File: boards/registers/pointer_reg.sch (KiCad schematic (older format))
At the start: 42 parts, among them U10 74ACT161, U11 74ACT244, U12 74ACT244, U13 74ACT161, U14 74ACT161, U15 74ACT244, U16 74ACT244, U9 74ACT161

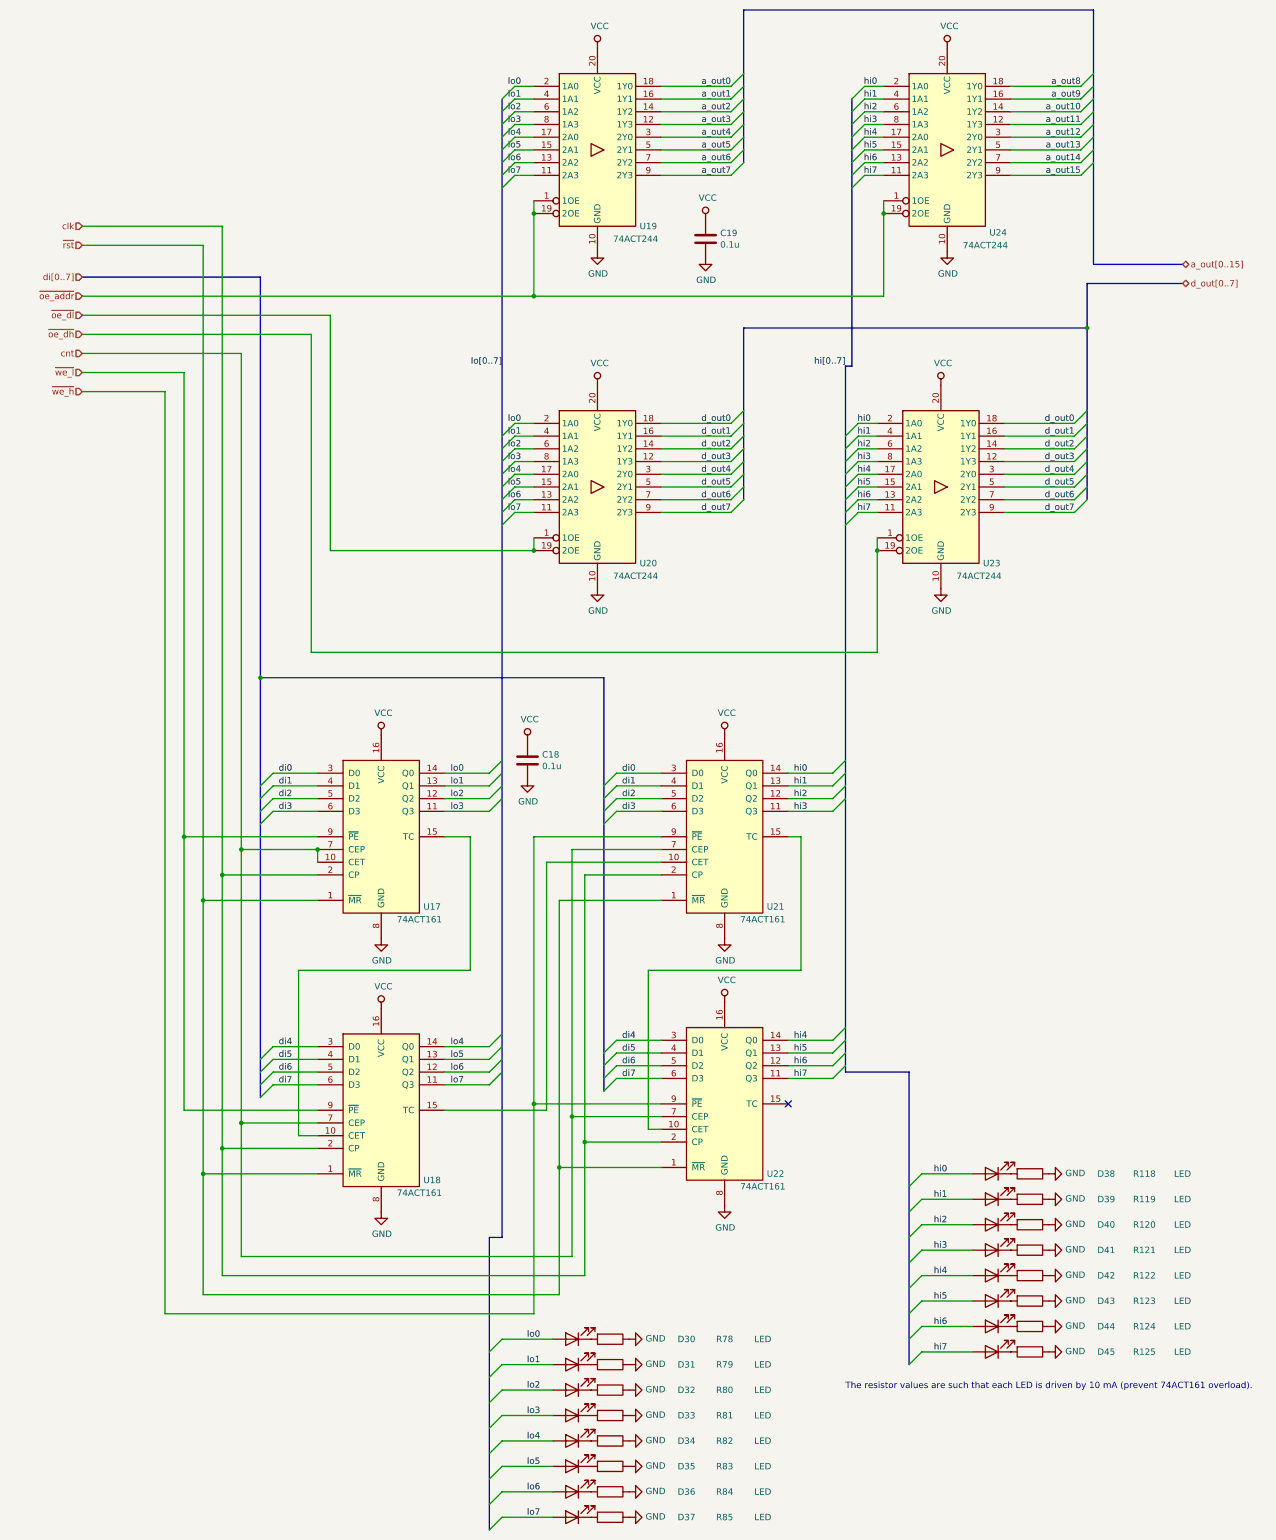
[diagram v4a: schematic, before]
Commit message: Remove RAM and ROM from the registers board, board rework in progress
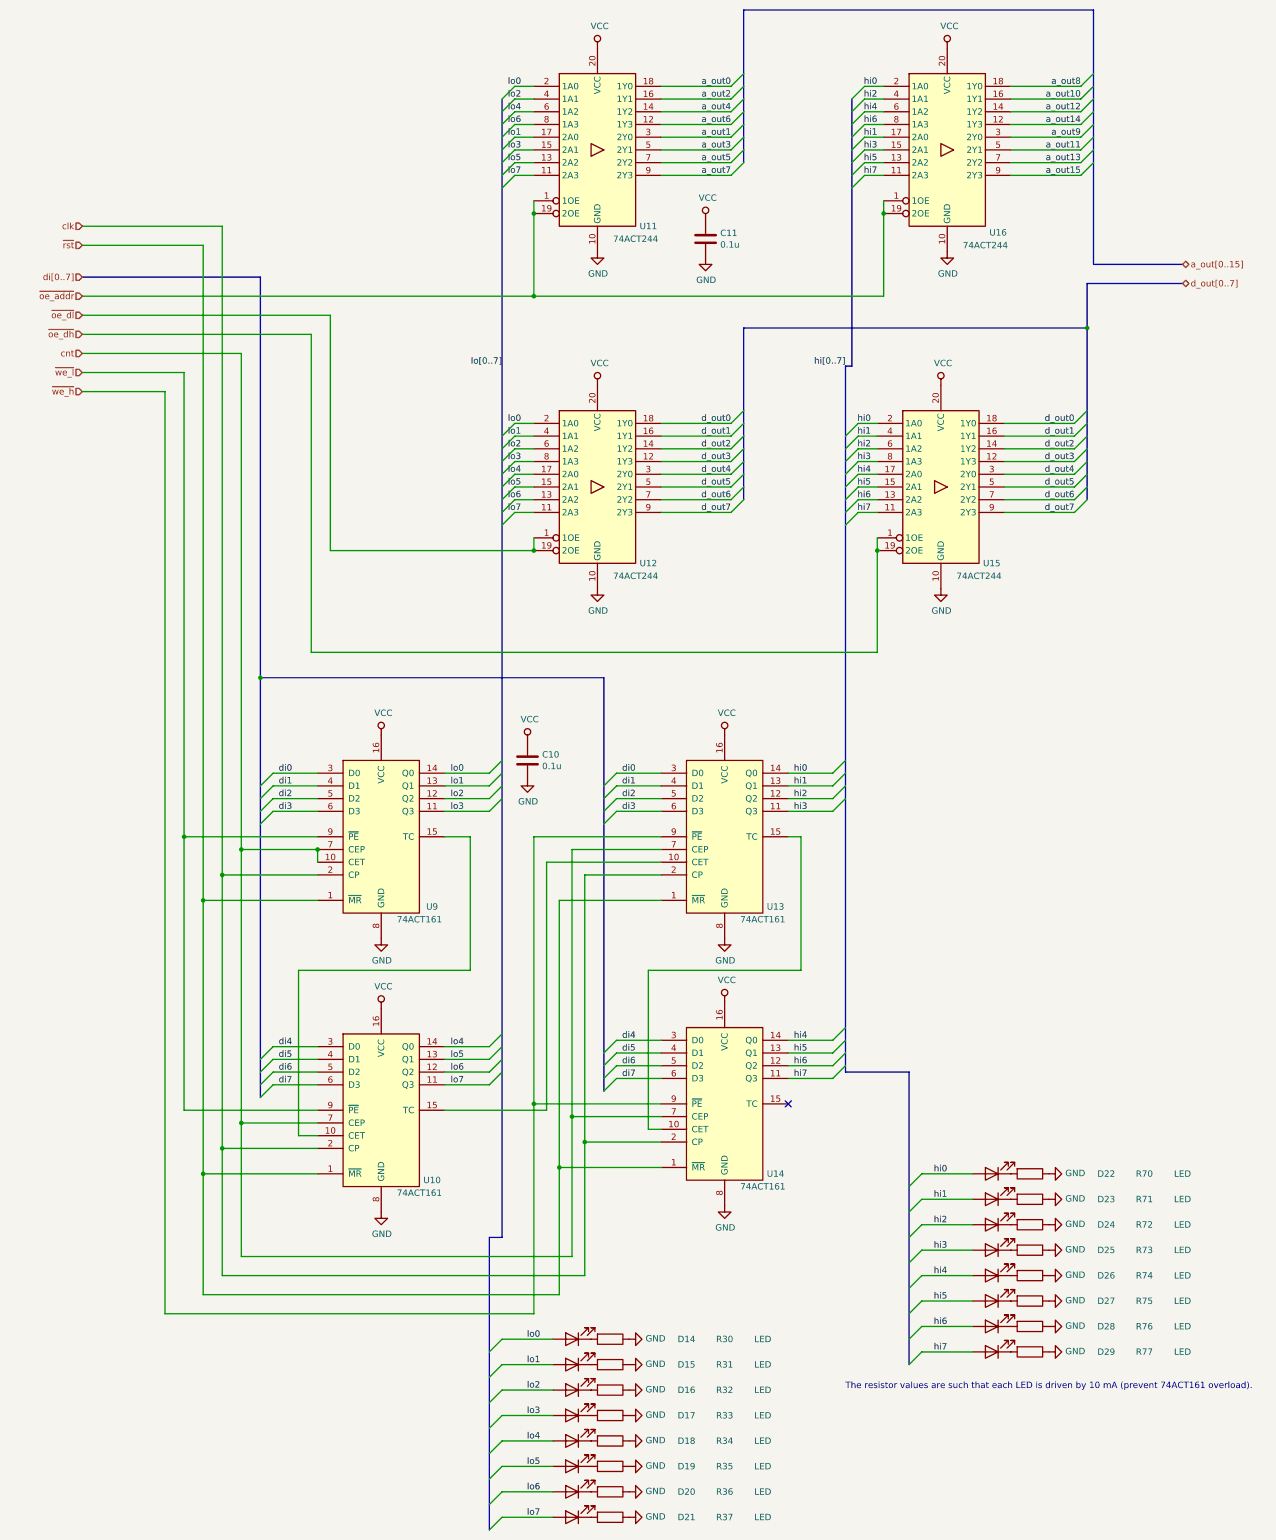
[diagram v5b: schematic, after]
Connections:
- net a_out1: now also U11.3 (2Y0); no longer U11.16 (1Y1)
- net a_out10: now also U16.16 (1Y1); no longer U16.14 (1Y2)
- net a_out11: now also U16.5 (2Y1); no longer U16.12 (1Y3)
- net a_out12: now also U16.14 (1Y2); no longer U16.3 (2Y0)
- net a_out13: now also U16.7 (2Y2); no longer U16.5 (2Y1)
- net a_out14: now also U16.12 (1Y3); no longer U16.7 (2Y2)
- net a_out2: now also U11.16 (1Y1); no longer U11.14 (1Y2)
- net a_out3: now also U11.5 (2Y1); no longer U11.12 (1Y3)
- net a_out4: now also U11.14 (1Y2); no longer U11.3 (2Y0)
- net a_out5: now also U11.7 (2Y2); no longer U11.5 (2Y1)
- net a_out6: now also U11.12 (1Y3); no longer U11.7 (2Y2)
- net a_out9: now also U16.3 (2Y0); no longer U16.16 (1Y1)
- net hi1: now also U16.17 (2A0); no longer U16.4 (1A1)
- net hi2: now also U16.4 (1A1); no longer U16.6 (1A2)
- net hi3: now also U16.15 (2A1); no longer U16.8 (1A3)
- net hi4: now also U16.6 (1A2); no longer U16.17 (2A0)
- net hi5: now also U16.13 (2A2); no longer U16.15 (2A1)
- net hi6: now also U16.8 (1A3); no longer U16.13 (2A2)
- net lo1: now also U11.17 (2A0); no longer U11.4 (1A1)
- net lo2: now also U11.4 (1A1); no longer U11.6 (1A2)
- net lo3: now also U11.15 (2A1); no longer U11.8 (1A3)
- net lo4: now also U11.6 (1A2); no longer U11.17 (2A0)
- net lo5: now also U11.13 (2A2); no longer U11.15 (2A1)
- net lo6: now also U11.8 (1A3); no longer U11.13 (2A2)

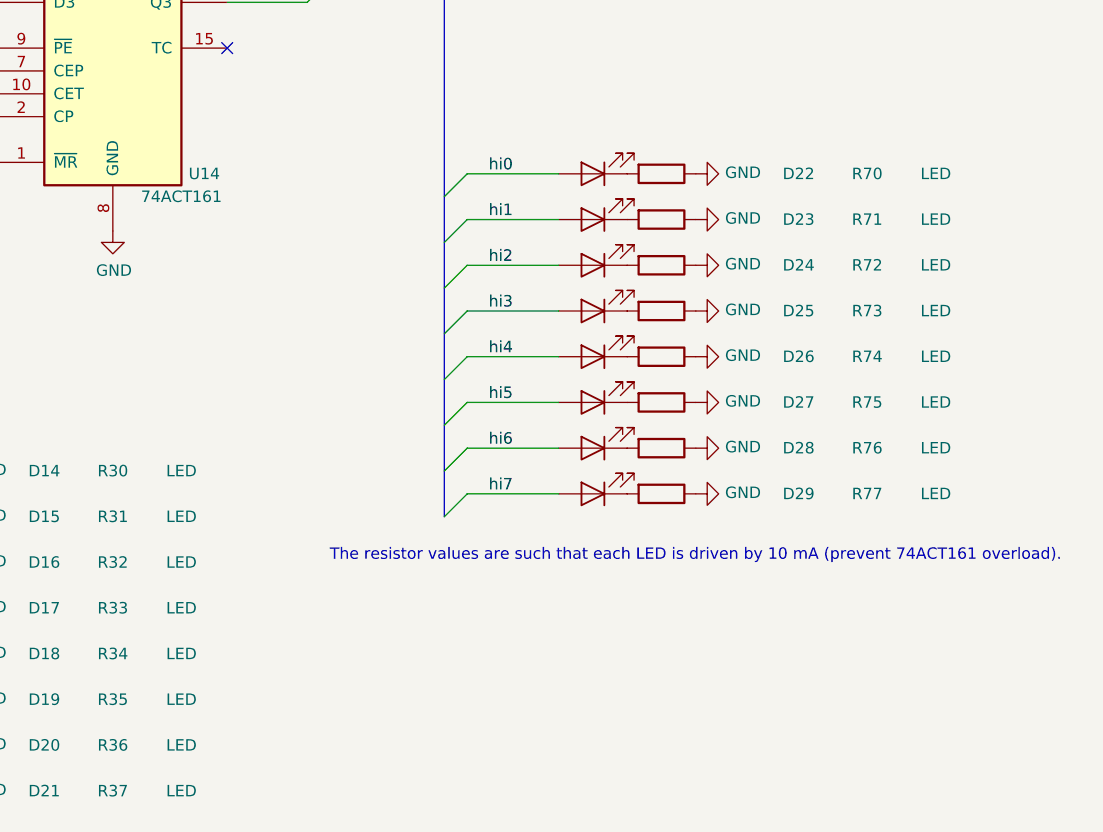
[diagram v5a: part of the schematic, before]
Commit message: LEDs and LED resistors
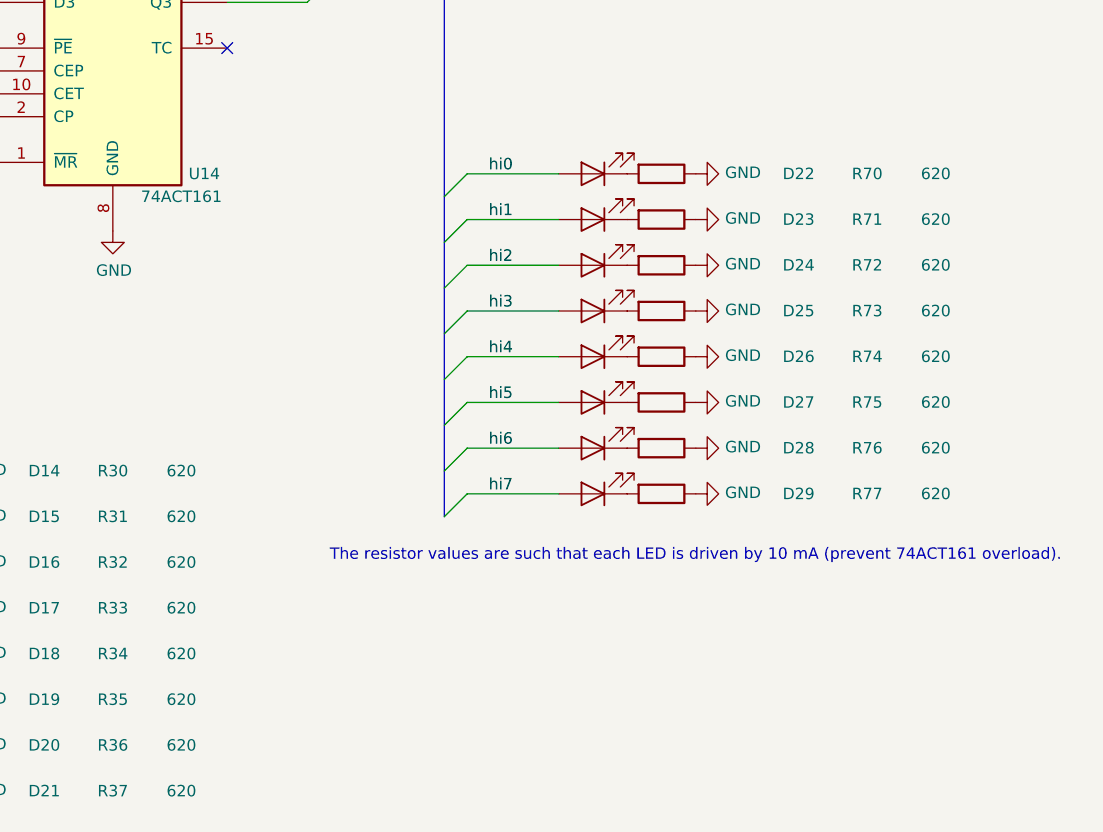
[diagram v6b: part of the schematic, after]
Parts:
- D14, D15, D16, D17, D18, D19, D20, D21, D22, D23, D24, D25, D26, D27, D28, D29: value LED0805 -> KP-2012EC
- R30, R31, R32, R33, R34, R35, R36, R37, R70, R71, R72, R73, R74, R75, R76, R77: value LED -> 620
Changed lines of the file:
@@
 AR Path="/5E0666E8/5E5C90D9/5E46F7D5" Ref="D32"  Part="1"
 F 0 "D16" H 4450 13600 50  0000 C CNN
-F 1 "LED0805" H 4050 13600 50  0001 C CNN
+F 1 "KP-2012EC" H 4050 13600 50  0001 C CNN
 F 2 "LED_SMD:LED_0805_2012Metric" H 5350 13600 50  0001 C CNN
 F 3 "~" H 5350 13600 50  0001 C CNN
@@
 AR Path="/5E0666E8/5E5C90D9/5E4730C4" Ref="R80"  Part="1"
 F 0 "R32" V 5650 14500 50  0000 C CNN
-F 1 "LED" V 5650 14800 50  0000 C CNN
+F 1 "620" V 5650 14800 50  0000 C CNN
 F 2 "Resistor_SMD:R_0805_2012Metric" V 5580 13600 50  0001 C CNN
 F 3 "~" H 5650 13600 50  0001 C CNN
@@
 AR Path="/5E0666E8/5E5C90D9/5E479607" Ref="D33"  Part="1"
 F 0 "D17" H 4450 13800 50  0000 C CNN
-F 1 "LED0805" H 4050 13800 50  0001 C CNN
+F 1 "KP-2012EC" H 4050 13800 50  0001 C CNN
 F 2 "LED_SMD:LED_0805_2012Metric" H 5350 13800 50  0001 C CNN
 F 3 "~" H 5350 13800 50  0001 C CNN
@@
 AR Path="/5E0666E8/5E5C90D9/5E47960D" Ref="R81"  Part="1"
 F 0 "R33" V 5650 14700 50  0000 C CNN
-F 1 "LED" V 5650 15000 50  0000 C CNN
+F 1 "620" V 5650 15000 50  0000 C CNN
 F 2 "Resistor_SMD:R_0805_2012Metric" V 5580 13800 50  0001 C CNN
 F 3 "~" H 5650 13800 50  0001 C CNN
@@
 AR Path="/5E0666E8/5E5C90D9/5E48763E" Ref="D34"  Part="1"
 F 0 "D18" H 4450 14000 50  0000 C CNN
-F 1 "LED0805" H 4050 14000 50  0001 C CNN
+F 1 "KP-2012EC" H 4050 14000 50  0001 C CNN
 F 2 "LED_SMD:LED_0805_2012Metric" H 5350 14000 50  0001 C CNN
 F 3 "~" H 5350 14000 50  0001 C CNN
@@
 AR Path="/5E0666E8/5E5C90D9/5E487644" Ref="R82"  Part="1"
 F 0 "R34" V 5650 14900 50  0000 C CNN
-F 1 "LED" V 5650 15200 50  0000 C CNN
+F 1 "620" V 5650 15200 50  0000 C CNN
 F 2 "Resistor_SMD:R_0805_2012Metric" V 5580 14000 50  0001 C CNN
 F 3 "~" H 5650 14000 50  0001 C CNN
@@
 AR Path="/5E0666E8/5E5C90D9/5E495EF5" Ref="D35"  Part="1"
 F 0 "D19" H 4450 14200 50  0000 C CNN
-F 1 "LED0805" H 4050 14200 50  0001 C CNN
+F 1 "KP-2012EC" H 4050 14200 50  0001 C CNN
 F 2 "LED_SMD:LED_0805_2012Metric" H 5350 14200 50  0001 C CNN
 F 3 "~" H 5350 14200 50  0001 C CNN
@@
 AR Path="/5E0666E8/5E5C90D9/5E495EFB" Ref="R83"  Part="1"
 F 0 "R35" V 5650 15100 50  0000 C CNN
-F 1 "LED" V 5650 15400 50  0000 C CNN
+F 1 "620" V 5650 15400 50  0000 C CNN
 F 2 "Resistor_SMD:R_0805_2012Metric" V 5580 14200 50  0001 C CNN
 F 3 "~" H 5650 14200 50  0001 C CNN
@@
 AR Path="/5E0666E8/5E5C90D9/5E4A452C" Ref="D36"  Part="1"
 F 0 "D20" H 4450 14400 50  0000 C CNN
-F 1 "LED0805" H 4050 14400 50  0001 C CNN
+F 1 "KP-2012EC" H 4050 14400 50  0001 C CNN
 F 2 "LED_SMD:LED_0805_2012Metric" H 5350 14400 50  0001 C CNN
 F 3 "~" H 5350 14400 50  0001 C CNN
@@
 AR Path="/5E0666E8/5E5C90D9/5E4A4532" Ref="R84"  Part="1"
 F 0 "R36" V 5650 15300 50  0000 C CNN
-F 1 "LED" V 5650 15600 50  0000 C CNN
+F 1 "620" V 5650 15600 50  0000 C CNN
 F 2 "Resistor_SMD:R_0805_2012Metric" V 5580 14400 50  0001 C CNN
 F 3 "~" H 5650 14400 50  0001 C CNN
@@
 AR Path="/5E0666E8/5E5C90D9/5E4B1F63" Ref="D31"  Part="1"
 F 0 "D15" H 4450 13400 50  0000 C CNN
-F 1 "LED0805" H 4050 13400 50  0001 C CNN
+F 1 "KP-2012EC" H 4050 13400 50  0001 C CNN
 F 2 "LED_SMD:LED_0805_2012Metric" H 5350 13400 50  0001 C CNN
 F 3 "~" H 5350 13400 50  0001 C CNN
@@
 AR Path="/5E0666E8/5E5C90D9/5E4B1F69" Ref="R79"  Part="1"
 F 0 "R31" V 5650 14300 50  0000 C CNN
-F 1 "LED" V 5650 14600 50  0000 C CNN
+F 1 "620" V 5650 14600 50  0000 C CNN
 F 2 "Resistor_SMD:R_0805_2012Metric" V 5580 13400 50  0001 C CNN
 F 3 "~" H 5650 13400 50  0001 C CNN
@@
 AR Path="/5E0666E8/5E5C90D9/5E4BF9DA" Ref="D30"  Part="1"
 F 0 "D14" H 4450 13200 50  0000 C CNN
-F 1 "LED0805" H 4050 13200 50  0001 C CNN
+F 1 "KP-2012EC" H 4050 13200 50  0001 C CNN
 F 2 "LED_SMD:LED_0805_2012Metric" H 5350 13200 50  0001 C CNN
 F 3 "~" H 5350 13200 50  0001 C CNN
@@
 AR Path="/5E0666E8/5E5C90D9/5E4BF9E0" Ref="R78"  Part="1"
 F 0 "R30" V 5650 14100 50  0000 C CNN
-F 1 "LED" V 5650 14400 50  0000 C CNN
+F 1 "620" V 5650 14400 50  0000 C CNN
 F 2 "Resistor_SMD:R_0805_2012Metric" V 5580 13200 50  0001 C CNN
 F 3 "~" H 5650 13200 50  0001 C CNN
@@
 AR Path="/5E0666E8/5E5C90D9/5E4CD491" Ref="D37"  Part="1"
 F 0 "D21" H 4450 14600 50  0000 C CNN
-F 1 "LED0805" H 4050 14600 50  0001 C CNN
+F 1 "KP-2012EC" H 4050 14600 50  0001 C CNN
 F 2 "LED_SMD:LED_0805_2012Metric" H 5350 14600 50  0001 C CNN
 F 3 "~" H 5350 14600 50  0001 C CNN
@@
 AR Path="/5E0666E8/5E5C90D9/5E4CD497" Ref="R85"  Part="1"
 F 0 "R37" V 5650 15500 50  0000 C CNN
-F 1 "LED" V 5650 15800 50  0000 C CNN
+F 1 "620" V 5650 15800 50  0000 C CNN
 F 2 "Resistor_SMD:R_0805_2012Metric" V 5580 14600 50  0001 C CNN
 F 3 "~" H 5650 14600 50  0001 C CNN
@@
 AR Path="/5E0666E8/5E5C90D9/5E59D0A3" Ref="D40"  Part="1"
 F 0 "D24" H 7750 12300 50  0000 C CNN
-F 1 "LED0805" H 7350 12300 50  0001 C CNN
+F 1 "KP-2012EC" H 7350 12300 50  0001 C CNN
 F 2 "LED_SMD:LED_0805_2012Metric" H 8650 12300 50  0001 C CNN
 F 3 "~" H 8650 12300 50  0001 C CNN
@@
 AR Path="/5E0666E8/5E5C90D9/5E59D0A9" Ref="R120"  Part="1"
 F 0 "R72" V 8950 13200 50  0000 C CNN
-F 1 "LED" V 8950 13500 50  0000 C CNN
+F 1 "620" V 8950 13500 50  0000 C CNN
 F 2 "Resistor_SMD:R_0805_2012Metric" V 8880 12300 50  0001 C CNN
 F 3 "~" H 8950 12300 50  0001 C CNN
@@
 AR Path="/5E0666E8/5E5C90D9/5E59D0B6" Ref="D41"  Part="1"
 F 0 "D25" H 7750 12500 50  0000 C CNN
-F 1 "LED0805" H 7350 12500 50  0001 C CNN
+F 1 "KP-2012EC" H 7350 12500 50  0001 C CNN
 F 2 "LED_SMD:LED_0805_2012Metric" H 8650 12500 50  0001 C CNN
 F 3 "~" H 8650 12500 50  0001 C CNN
@@
 AR Path="/5E0666E8/5E5C90D9/5E59D0BC" Ref="R121"  Part="1"
 F 0 "R73" V 8950 13400 50  0000 C CNN
-F 1 "LED" V 8950 13700 50  0000 C CNN
+F 1 "620" V 8950 13700 50  0000 C CNN
 F 2 "Resistor_SMD:R_0805_2012Metric" V 8880 12500 50  0001 C CNN
 F 3 "~" H 8950 12500 50  0001 C CNN
@@
 AR Path="/5E0666E8/5E5C90D9/5E59D0C9" Ref="D42"  Part="1"
 F 0 "D26" H 7750 12700 50  0000 C CNN
-F 1 "LED0805" H 7350 12700 50  0001 C CNN
+F 1 "KP-2012EC" H 7350 12700 50  0001 C CNN
 F 2 "LED_SMD:LED_0805_2012Metric" H 8650 12700 50  0001 C CNN
 F 3 "~" H 8650 12700 50  0001 C CNN
@@
 AR Path="/5E0666E8/5E5C90D9/5E59D0CF" Ref="R122"  Part="1"
 F 0 "R74" V 8950 13600 50  0000 C CNN
-F 1 "LED" V 8950 13900 50  0000 C CNN
+F 1 "620" V 8950 13900 50  0000 C CNN
 F 2 "Resistor_SMD:R_0805_2012Metric" V 8880 12700 50  0001 C CNN
 F 3 "~" H 8950 12700 50  0001 C CNN
@@
 AR Path="/5E0666E8/5E5C90D9/5E59D0DC" Ref="D43"  Part="1"
 F 0 "D27" H 7750 12900 50  0000 C CNN
-F 1 "LED0805" H 7350 12900 50  0001 C CNN
+F 1 "KP-2012EC" H 7350 12900 50  0001 C CNN
 F 2 "LED_SMD:LED_0805_2012Metric" H 8650 12900 50  0001 C CNN
 F 3 "~" H 8650 12900 50  0001 C CNN
@@
 AR Path="/5E0666E8/5E5C90D9/5E59D0E2" Ref="R123"  Part="1"
 F 0 "R75" V 8950 13800 50  0000 C CNN
-F 1 "LED" V 8950 14100 50  0000 C CNN
+F 1 "620" V 8950 14100 50  0000 C CNN
 F 2 "Resistor_SMD:R_0805_2012Metric" V 8880 12900 50  0001 C CNN
 F 3 "~" H 8950 12900 50  0001 C CNN
@@
 AR Path="/5E0666E8/5E5C90D9/5E59D0EF" Ref="D44"  Part="1"
 F 0 "D28" H 7750 13100 50  0000 C CNN
-F 1 "LED0805" H 7350 13100 50  0001 C CNN
+F 1 "KP-2012EC" H 7350 13100 50  0001 C CNN
 F 2 "LED_SMD:LED_0805_2012Metric" H 8650 13100 50  0001 C CNN
 F 3 "~" H 8650 13100 50  0001 C CNN
@@
 AR Path="/5E0666E8/5E5C90D9/5E59D0F5" Ref="R124"  Part="1"
 F 0 "R76" V 8950 14000 50  0000 C CNN
-F 1 "LED" V 8950 14300 50  0000 C CNN
+F 1 "620" V 8950 14300 50  0000 C CNN
 F 2 "Resistor_SMD:R_0805_2012Metric" V 8880 13100 50  0001 C CNN
 F 3 "~" H 8950 13100 50  0001 C CNN
@@
 AR Path="/5E0666E8/5E5C90D9/5E59D102" Ref="D39"  Part="1"
 F 0 "D23" H 7750 12100 50  0000 C CNN
-F 1 "LED0805" H 7350 12100 50  0001 C CNN
+F 1 "KP-2012EC" H 7350 12100 50  0001 C CNN
 F 2 "LED_SMD:LED_0805_2012Metric" H 8650 12100 50  0001 C CNN
 F 3 "~" H 8650 12100 50  0001 C CNN
@@
 AR Path="/5E0666E8/5E5C90D9/5E59D108" Ref="R119"  Part="1"
 F 0 "R71" V 8950 13000 50  0000 C CNN
-F 1 "LED" V 8950 13300 50  0000 C CNN
+F 1 "620" V 8950 13300 50  0000 C CNN
 F 2 "Resistor_SMD:R_0805_2012Metric" V 8880 12100 50  0001 C CNN
 F 3 "~" H 8950 12100 50  0001 C CNN
@@
 AR Path="/5E0666E8/5E5C90D9/5E59D115" Ref="D38"  Part="1"
 F 0 "D22" H 7750 11900 50  0000 C CNN
-F 1 "LED0805" H 7350 11900 50  0001 C CNN
+F 1 "KP-2012EC" H 7350 11900 50  0001 C CNN
 F 2 "LED_SMD:LED_0805_2012Metric" H 8650 11900 50  0001 C CNN
 F 3 "~" H 8650 11900 50  0001 C CNN
@@
 AR Path="/5E0666E8/5E5C90D9/5E59D11B" Ref="R118"  Part="1"
 F 0 "R70" V 8950 12800 50  0000 C CNN
-F 1 "LED" V 8950 13100 50  0000 C CNN
+F 1 "620" V 8950 13100 50  0000 C CNN
 F 2 "Resistor_SMD:R_0805_2012Metric" V 8880 11900 50  0001 C CNN
 F 3 "~" H 8950 11900 50  0001 C CNN
@@
 AR Path="/5E0666E8/5E5C90D9/5E59D128" Ref="D45"  Part="1"
 F 0 "D29" H 7750 13300 50  0000 C CNN
-F 1 "LED0805" H 7350 13300 50  0001 C CNN
+F 1 "KP-2012EC" H 7350 13300 50  0001 C CNN
 F 2 "LED_SMD:LED_0805_2012Metric" H 8650 13300 50  0001 C CNN
 F 3 "~" H 8650 13300 50  0001 C CNN
@@
 AR Path="/5E0666E8/5E5C90D9/5E59D12E" Ref="R125"  Part="1"
 F 0 "R77" V 8950 14200 50  0000 C CNN
-F 1 "LED" V 8950 14500 50  0000 C CNN
+F 1 "620" V 8950 14500 50  0000 C CNN
 F 2 "Resistor_SMD:R_0805_2012Metric" V 8880 13300 50  0001 C CNN
 F 3 "~" H 8950 13300 50  0001 C CNN

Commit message: Part names
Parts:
- U10, U13, U14, U9: value 74ACT161 -> MC74ACT161DG
- U11, U12, U15, U16: value 74ACT244 -> SN74ACT244PW
